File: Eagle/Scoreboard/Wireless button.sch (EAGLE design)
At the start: 24 parts, among them Q1 2N3904, Q2 IRF9530

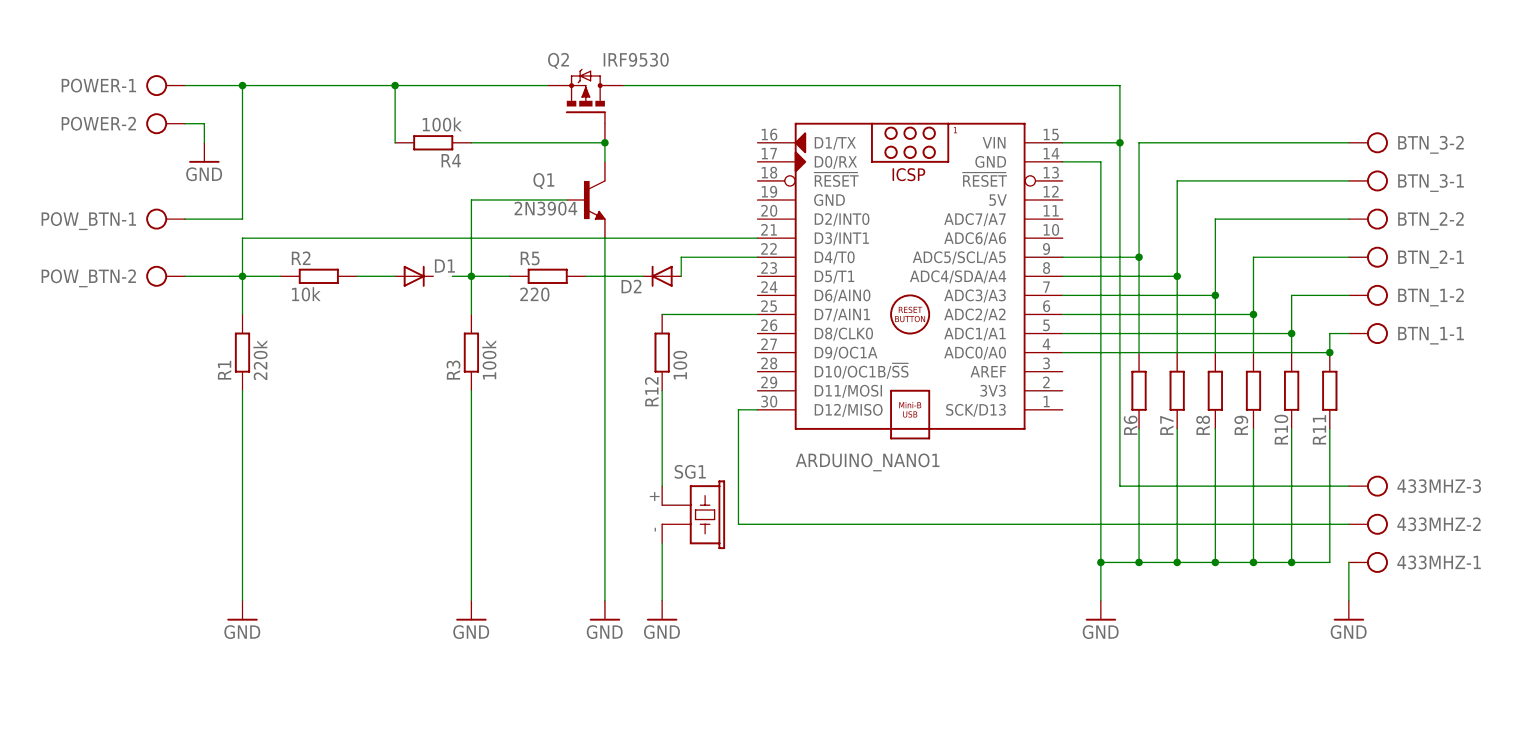
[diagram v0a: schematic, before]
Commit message: Updated scheme and added board. Pins are not zet aligned with code
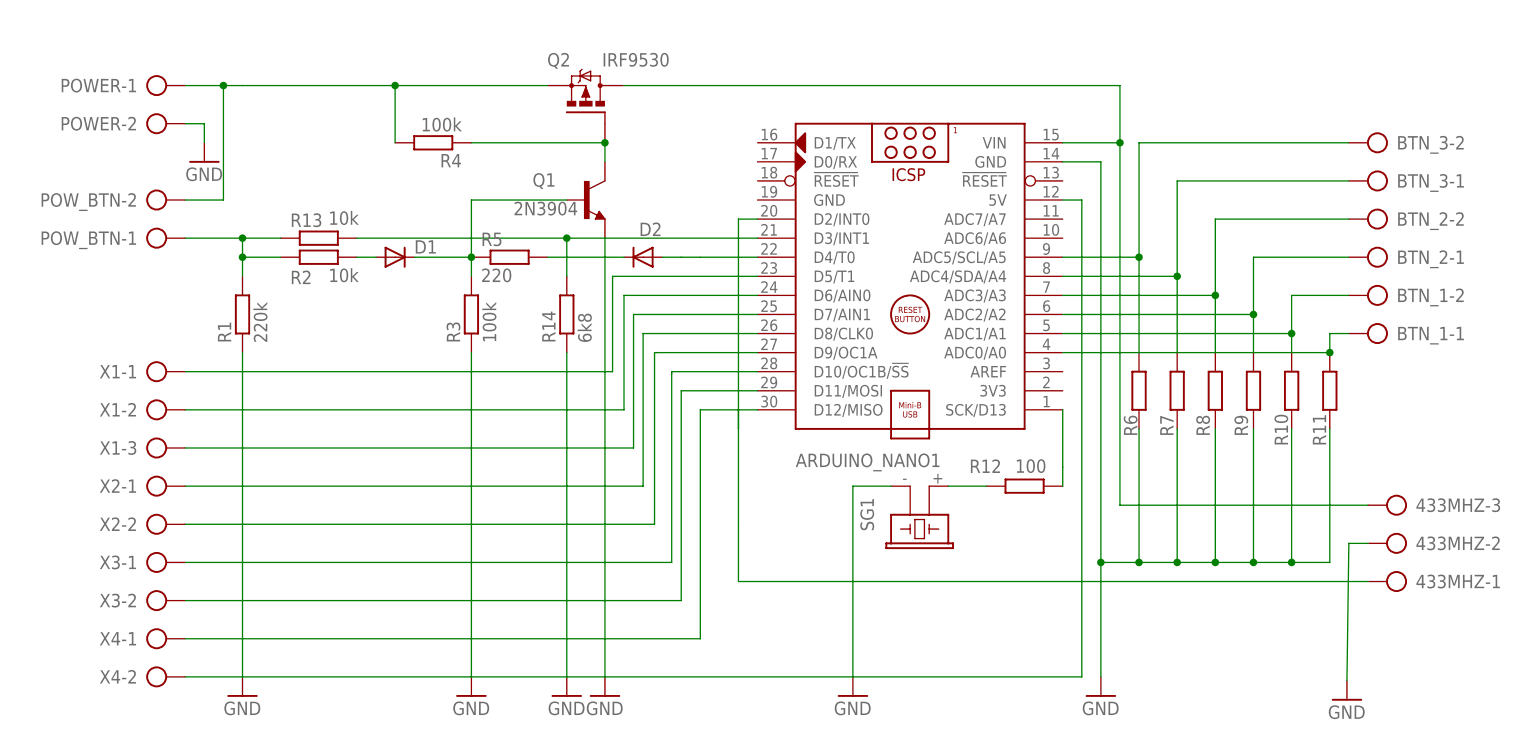
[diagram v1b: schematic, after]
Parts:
- added R13: 10k, resistor:R-EU_0207/7
- added R14: 6k8, resistor:R-EU_0207/7
- added X1: (no value), con-ptr500:AK500/3
- added X2, X3, X4: (no value), con-ptr500:AK500/2
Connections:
- net N$7 renamed VCC
- removed net N$1 (its old number): POWER-1.KL, POW_BTN-1.KL, Q2.S, R4.2
- new net 433_IN: 433MHZ-1.KL, ARDUINO_NANO1.D2/INT0
- new net 5V: ARDUINO_NANO1.5V, X4-2.KL
- new net BUZZ: ARDUINO_NANO1.SCK/D13, R12.2
- new net N$17: ARDUINO_NANO1.D9/OC1A, X2-2.KL
- new net N$18: ARDUINO_NANO1.D10/OC1B/!SS, X3-1.KL
- new net N$19: ARDUINO_NANO1.D11/MOSI, X3-2.KL
- new net N$20: ARDUINO_NANO1.D12/MISO, X4-1.KL
- new net N$7: ARDUINO_NANO1.D6/AIN0, X1-2.KL
- new net N$8: ARDUINO_NANO1.D7/AIN1, X1-3.KL
- new net OFF: POW_BTN-1.KL, R1.2, R13.1, R2.1
- new net POWER: POWER-1.KL, POW_BTN-2.KL, Q2.S, R4.2
- net GND: now also 433MHZ-2.KL, R14.1; no longer 433MHZ-1.KL
- net N$15: now also ARDUINO_NANO1.D8/CLK0, X2-1.KL; no longer ARDUINO_NANO1.D7/AIN1, R12.2
- net N$22: now also ARDUINO_NANO1.D3/INT1, R13.2, R14.2; no longer 433MHZ-2.KL, ARDUINO_NANO1.D12/MISO
- net N$3: now also ARDUINO_NANO1.D5/T1, X1-1.KL; no longer ARDUINO_NANO1.D3/INT1, POW_BTN-2.KL, R1.2, R2.1
- net N$5: now also D1.C
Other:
- moved on the sheet: 433MHZ-1, 433MHZ-2, 433MHZ-3, D1, D2, POW_BTN-1, POW_BTN-2, R1, R12, R2, R3, R5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

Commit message: Power for 433Mhz transmitter taking from 5V
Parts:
- removed X3, X4: (no value), con-ptr500:AK500/2
- added 5V, X5: (no value), con-ptr500:AK500/3
- R10, R11, R6, R7, R8, R9: value (none) -> 10k
- SG1: value F/CM12P -> F/EE17P; device buzzer:F/CM12P -> buzzer:F/EE17P
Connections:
- net 433_IN renamed N$10
- net N$10 renamed AWAY_UP
- net N$11 renamed AWAY_DOWN
- net N$12 renamed HOME_UP
- net N$13 renamed HOME_DOWN
- net N$14 renamed SWAP
- net N$16 renamed RESET
- net 5V: now also 433MHZ-3.KL, 5V-1.KL, 5V-2.KL, 5V-3.KL; no longer X4-2.KL
- net N$18: now also X5-1.KL; no longer X3-1.KL
- net N$19: now also X5-2.KL; no longer X3-2.KL
- net N$20: now also X5-3.KL; no longer X4-1.KL
- net VCC: no longer 433MHZ-3.KL
